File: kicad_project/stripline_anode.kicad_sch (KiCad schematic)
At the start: 31 parts, among them J1 QRM8-078-05.0-L-D-A, U1 anode_pad, U10 anode_pad, U11 anode_pad, U12 anode_pad, U13 anode_pad, U14 anode_pad, U15 anode_pad, U16 anode_pad, U17 anode_pad, U18 anode_pad, U19 anode_pad, U2 anode_pad, U20 anode_pad, U21 anode_pad, U22 anode_pad, U23 anode_pad, U24 anode_pad, U25 anode_pad, U26 anode_pad, U27 anode_pad, U28 anode_pad, U29 anode_pad, U3 anode_pad, U30 anode_pad, U4 anode_pad, U5 anode_pad, U6 anode_pad, U7 anode_pad, U8 anode_pad, U9 anode_pad

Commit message: managed footprints into a proper pretty library
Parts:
- U1, U2, U29, U3, U4: value anode_pad -> (none); footprint AnodePads:stripline_30 -> (none)
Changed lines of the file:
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@@
     (in_bom yes) (on_board yes)
     (property "Reference" "U1" (id 0) (at 40.132 26.67 0))
-    (property "Value" "anode_pad" (id 1) (at 29.718 29.21 0)
-      (effects (font (size 1.27 1.27)) hide)
-    )
-    (property "Footprint" "AnodePads:stripline_30" (id 2) (at 41.91 29.21 0)
+    (property "Value" "" (id 1) (at 29.718 29.21 0)
+      (effects (font (size 1.27 1.27)) hide)
+    )
+    (property "Footprint" "" (id 2) (at 41.91 29.21 0)
       (effects (font (size 1.27 1.27)) hide)
     )
@@
     (in_bom yes) (on_board yes)
     (property "Reference" "U2" (id 0) (at 39.37 33.274 0))
-    (property "Value" "anode_pad" (id 1) (at 29.464 35.814 0)
-      (effects (font (size 1.27 1.27)) hide)
-    )
-    (property "Footprint" "AnodePads:stripline_30" (id 2) (at 41.91 35.56 0)
+    (property "Value" "" (id 1) (at 29.464 35.814 0)
+      (effects (font (size 1.27 1.27)) hide)
+    )
+    (property "Footprint" "" (id 2) (at 41.91 35.56 0)
       (effects (font (size 1.27 1.27)) hide)
     )
@@
     (in_bom yes) (on_board yes)
     (property "Reference" "U3" (id 0) (at 39.37 39.878 0))
-    (property "Value" "anode_pad" (id 1) (at 29.464 41.91 0)
-      (effects (font (size 1.27 1.27)) hide)
-    )
-    (property "Footprint" "AnodePads:stripline_30" (id 2) (at 41.91 41.91 0)
+    (property "Value" "" (id 1) (at 29.464 41.91 0)
+      (effects (font (size 1.27 1.27)) hide)
+    )
+    (property "Footprint" "" (id 2) (at 41.91 41.91 0)
       (effects (font (size 1.27 1.27)) hide)
     )
@@
     (in_bom yes) (on_board yes)
     (property "Reference" "U4" (id 0) (at 39.116 45.974 0))
-    (property "Value" "anode_pad" (id 1) (at 29.972 48.006 0)
-      (effects (font (size 1.27 1.27)) hide)
-    )
-    (property "Footprint" "AnodePads:stripline_30" (id 2) (at 41.91 48.26 0)
+    (property "Value" "" (id 1) (at 29.972 48.006 0)
+      (effects (font (size 1.27 1.27)) hide)
+    )
+    (property "Footprint" "" (id 2) (at 41.91 48.26 0)
       (effects (font (size 1.27 1.27)) hide)
     )
@@
     (in_bom yes) (on_board yes)
     (property "Reference" "U29" (id 0) (at 84.836 76.708 0))
-    (property "Value" "anode_pad" (id 1) (at 80.772 79.756 0)
-      (effects (font (size 1.27 1.27)) hide)
-    )
-    (property "Footprint" "AnodePads:stripline_30" (id 2) (at 87.63 80.01 0)
+    (property "Value" "" (id 1) (at 80.772 79.756 0)
+      (effects (font (size 1.27 1.27)) hide)
+    )
+    (property "Footprint" "" (id 2) (at 87.63 80.01 0)
       (effects (font (size 1.27 1.27)) hide)
     )
@@
     )
     (path "/00000000-0000-0000-0000-0000618b32ee"
-      (reference "U1") (unit 1) (value "anode_pad") (footprint "AnodePads:stripline_30")
+      (reference "U1") (unit 1) (value "anode_pad") (footprint "LAPPD-readouts:stripline_30")
     )
     (path "/00000000-0000-0000-0000-0000618b32f7"
-      (reference "U2") (unit 1) (value "anode_pad") (footprint "AnodePads:stripline_30")
+      (reference "U2") (unit 1) (value "anode_pad") (footprint "LAPPD-readouts:stripline_30")
     )
     (path "/00000000-0000-0000-0000-0000618b3300"
-      (reference "U3") (unit 1) (value "anode_pad") (footprint "AnodePads:stripline_30")
+      (reference "U3") (unit 1) (value "anode_pad") (footprint "LAPPD-readouts:stripline_30")
     )
     (path "/00000000-0000-0000-0000-0000618b3309"
-      (reference "U4") (unit 1) (value "anode_pad") (footprint "AnodePads:stripline_30")
+      (reference "U4") (unit 1) (value "anode_pad") (footprint "LAPPD-readouts:stripline_30")
     )
     (path "/00000000-0000-0000-0000-0000618b3312"

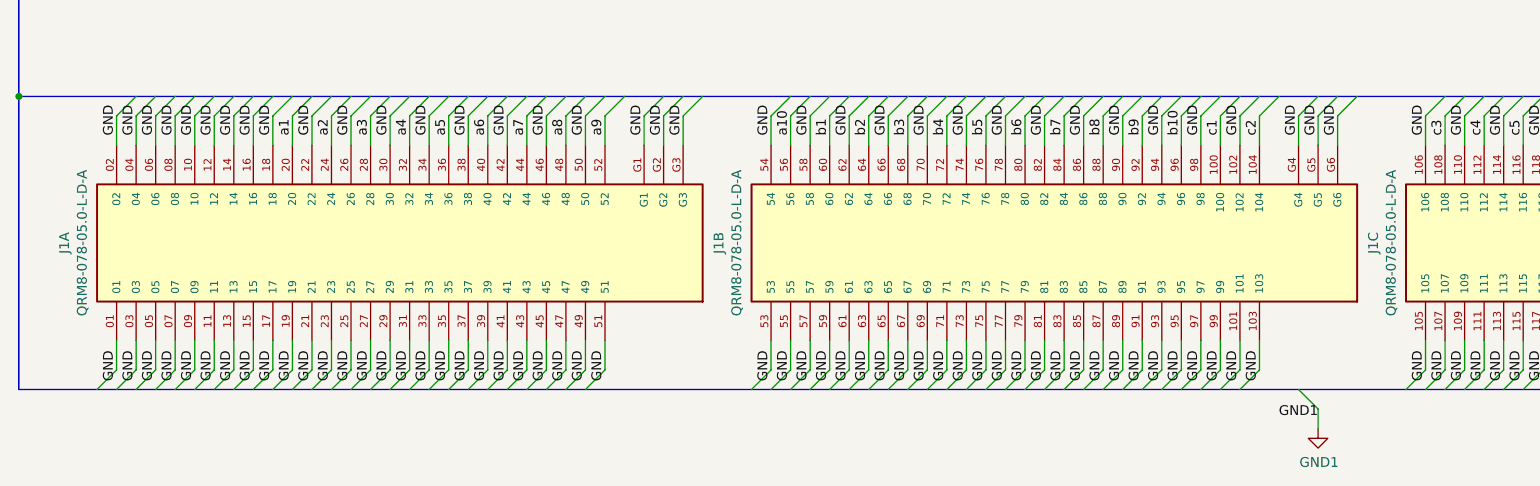
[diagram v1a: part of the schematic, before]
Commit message: Changed footprints to match new local footprint library. Redid edge cuts and user-drawings layer to have a well-positioning of ultem frame mounting holes. Put in four of those mounting holes, a few more to go. Put a rough edge-cuts layer (not positioned) so that copper pours work
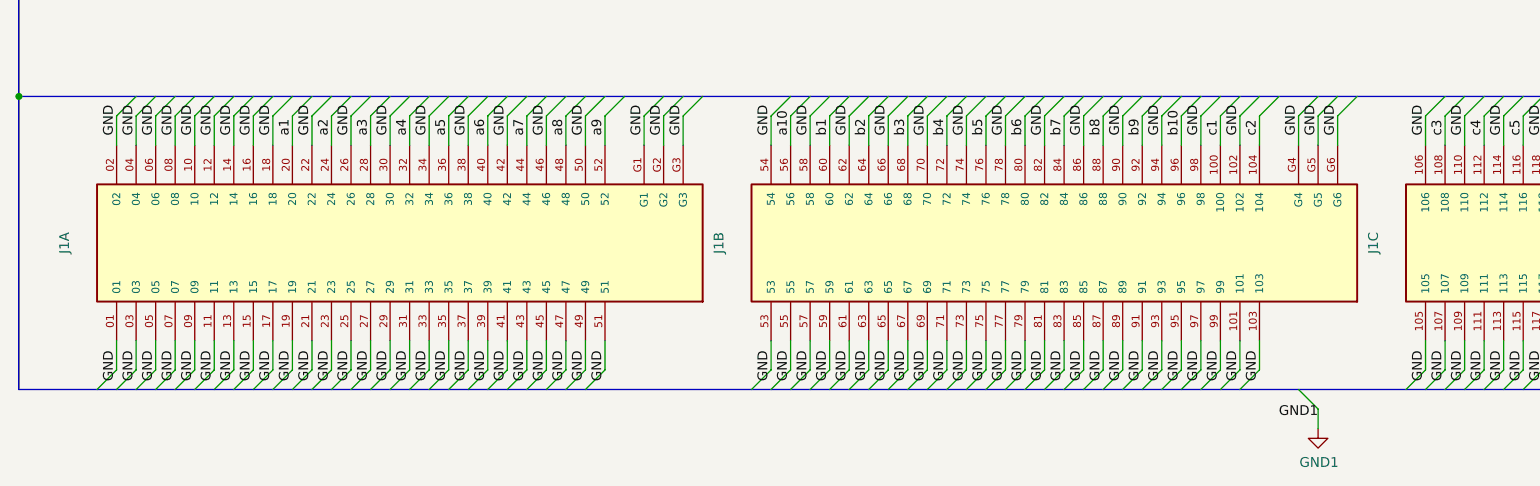
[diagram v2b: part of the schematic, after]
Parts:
- J1: value QRM8-078-05.0-L-D-A -> (none); footprint samtec-appsupport:SAMTEC_QRM8-078-05.0-L-D-A -> (none)
- U10, U11, U12, U13, U14, U15, U16, U17, U18, U19, U20, U21, U22, U23, U24, U25, U26, U27, U28, U30, U5, U6, U7, U8, U9: value anode_pad -> (none); footprint AnodePads:stripline_30 -> (none)

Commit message: Schematic added for HV circuit draft 1
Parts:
- added C?: (no value), symbol Device:C_Small
- added POGO? (x7): Conn_01x01, symbol Connector_Generic:Conn_01x01
- added POGO?: (no value), symbol Connector_Generic:Conn_01x01
- J1: value (none) -> QRM8-078-05.0-L-D-A; footprint (none) -> stripline-anode-footprints:SAMTEC_QRM8-078-05.0-L-D-A
- U1, U10, U11, U12, U13, U14, U15, U16, U17, U18, U19, U20, U21, U22, U23, U24, U25, U26, U27, U28, U29, U3, U30, U4, U5, U6, U7, U8, U9: value (none) -> anode_pad; footprint (none) -> stripline-anode-footprints:stripline_30
- U2: value (none) -> anode_pad; footprint (none) -> LAPPD-readouts:stripline_30
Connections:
- net GND: now also C?.2
- new net High voltage distribution/sup_gnd: C?.1, POGO?.1 (Pin_1), POGO?.1 (Pin_1), POGO?.1 (Pin_1), POGO?.1 (Pin_1), POGO?.1 (Pin_1), POGO?.1 (Pin_1), POGO?.1 (Pin_1), POGO?.1 (Pin_1)
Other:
- added sheet High voltage distribution (hv-distribution.kicad_sch)
- note added: "Pogo pins make contact with the internal LAPPD anode coating at the rim, and also at the readout board, a point of ground connection for the internal anode"

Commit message: Schematic done for HV-circuit. Would like to merge before making layout changes, as some layout changes have been made on other branch and I'm not sure how it will be handled in git
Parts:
- removed POGO? (x4): Conn_01x01, symbol Connector_Generic:Conn_01x01
- added C?: (no value), symbol Device:C_Small
- POGO? (x3): value Conn_01x01 -> (none)
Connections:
- net GND: now also C?.2
- net High voltage distribution/sup_gnd: now also C?.1
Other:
- moved on the sheet: C?

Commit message: First draft layout of HV circuit. Things to refine: (1) ground return pads / mounting holes for gnd return. (2) Idea of how the high voltage inputs/outputs actually hook up to the LAPPD and incoming cables. (3) UL796 standard has 1.6kV/mm rating on distances between conductors. Is this tolerance actually OK, considering the present layout of gnd pour. (4) Do all of the components clear mechanical constraints of the LAPPD and Ultem frame, i.e. we wont have a solder mound where the detector or frame needs to be flush.
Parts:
- C1, C2: renamed from C?; value (none) -> 0.1 uF; footprint (none) -> Capacitor_THT:C_Disc_D3.0mm_W1.6mm_P2.50mm
- POGO1, POGO2, POGO3, POGO4: renamed from POGO?; value (none) -> Conn_01x01; footprint (none) -> MountingHole:MountingHole_2.5mm_Pad

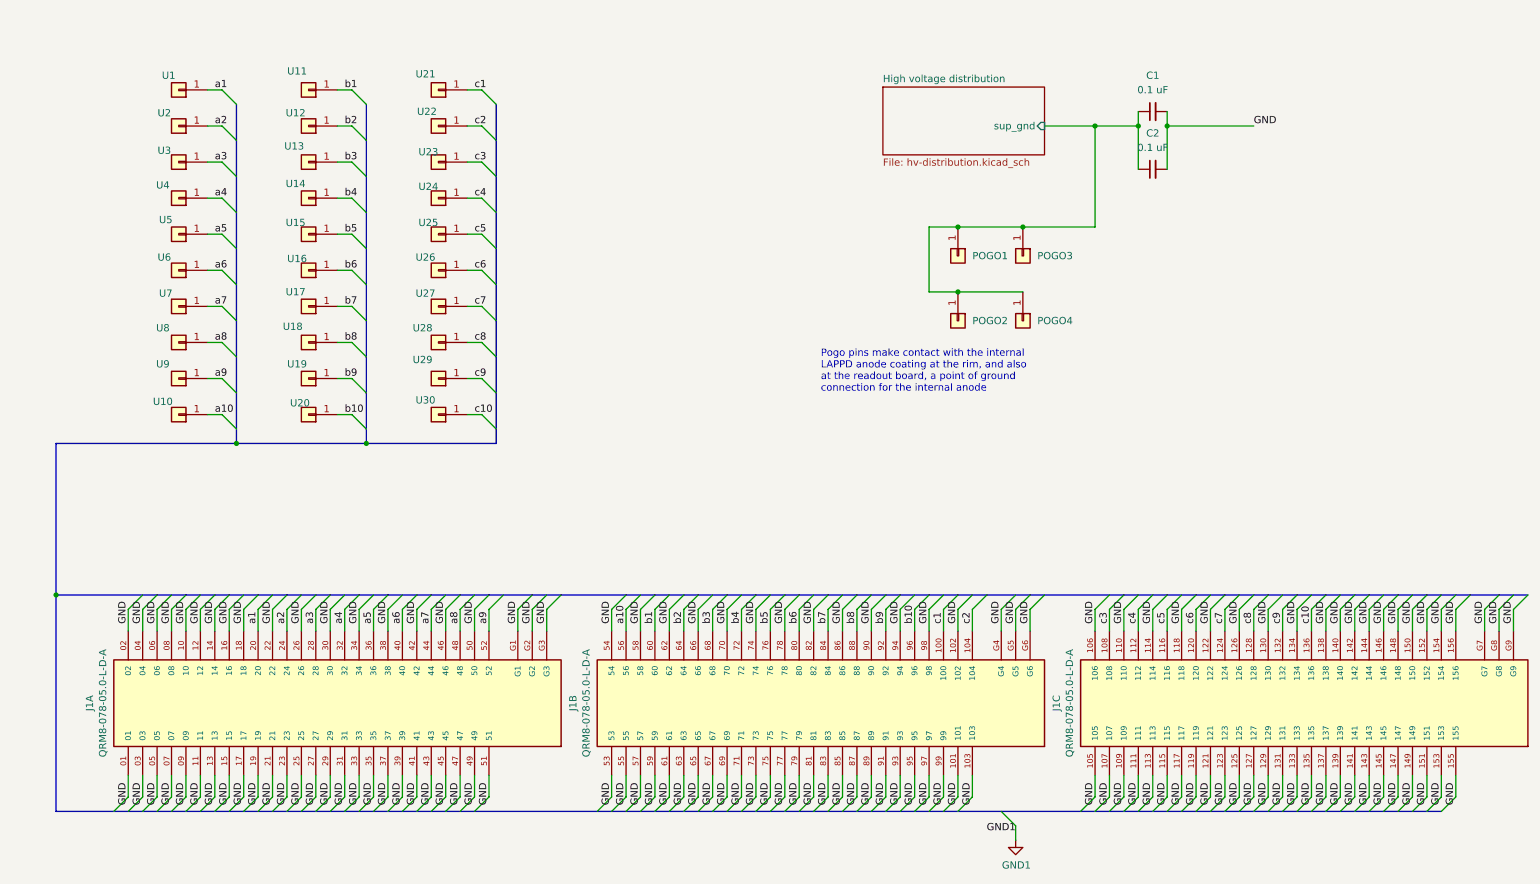
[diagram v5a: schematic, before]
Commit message: A close to final version of high voltage circuitry, after having decided to go with SHV cable ends soldered on to SMD pads, potted, and strain relieved by zip ties. Also added SMA ports. This is one day before meeting to review
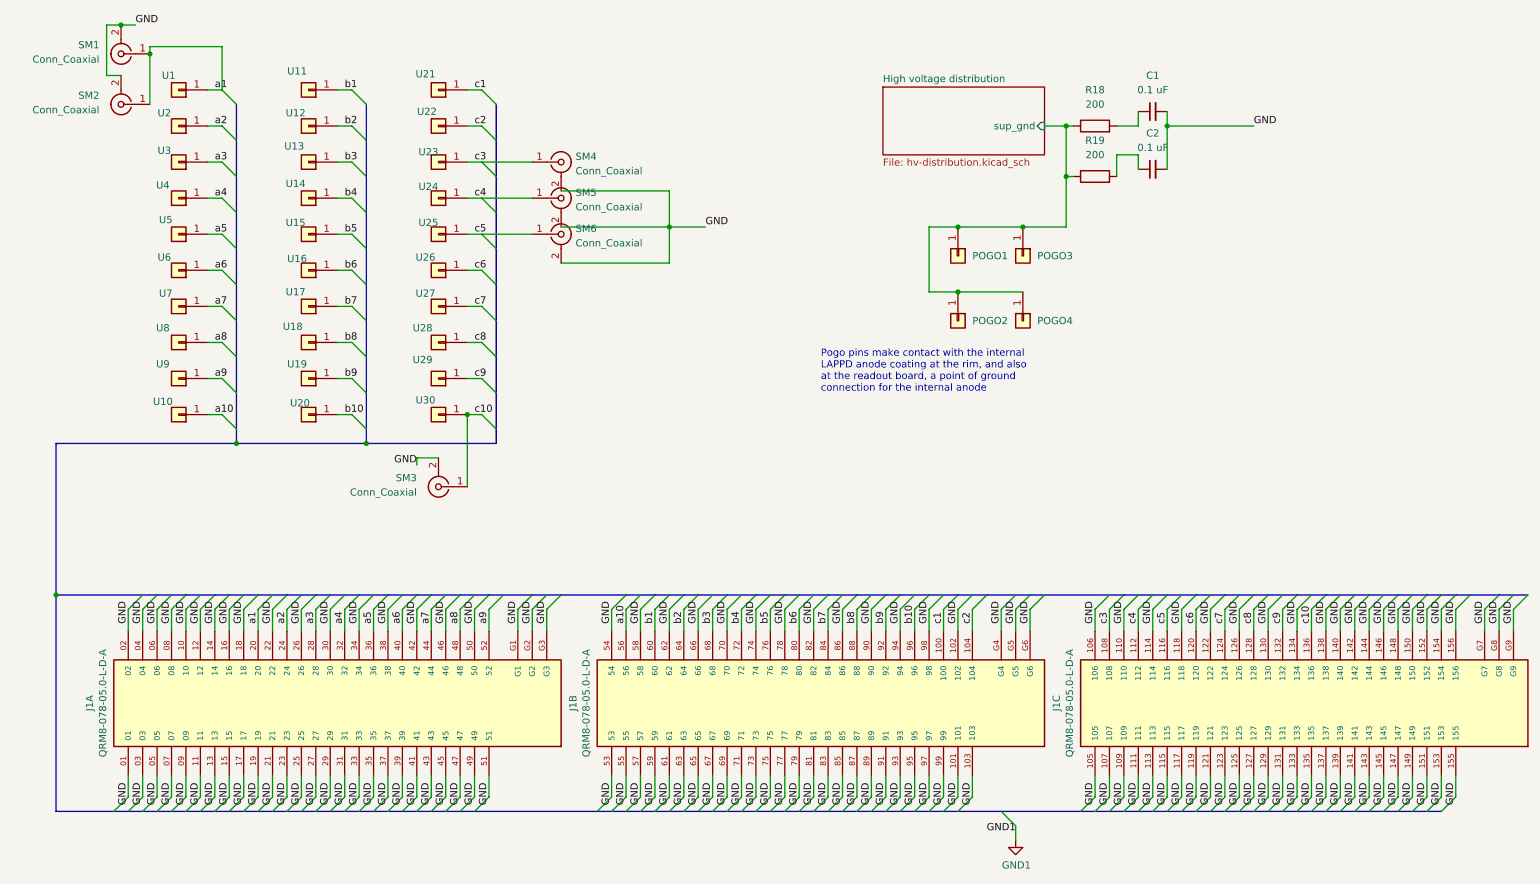
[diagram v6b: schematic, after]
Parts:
- added R18, R19: 200, Resistor_SMD:R_2512_6332Metric_Pad1.40x3.35mm_HandSolder, symbol Device:R
- added SM1, SM2, SM3, SM4, SM5, SM6: Conn_Coaxial, Connector_Coaxial:SMA_Johnson_142-0711-271, symbol Connector:Conn_Coaxial
- C1, C2: footprint Capacitor_THT:C_Disc_D3.0mm_W1.6mm_P2.50mm -> Capacitor_SMD:C_1812_4532Metric_Pad1.57x3.40mm_HandSolder
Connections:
- net GND: now also SM1.2 (Ext), SM2.2 (Ext), SM3.2 (Ext), SM4.2 (Ext), SM5.2 (Ext), SM6.2 (Ext)
- net High voltage distribution/sup_gnd: now also R18.1, R19.1; no longer C1.1, C2.1
- net a1: now also SM1.1 (In), SM2.1 (In)
- net c10: now also SM3.1 (In)
- net c3: now also SM4.1 (In)
- net c4: now also SM5.1 (In)
- net c5: now also SM6.1 (In)
- new net: C2.1, R19.2
- new net: C1.1, R18.2
